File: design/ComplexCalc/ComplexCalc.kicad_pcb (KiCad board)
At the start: 2 copper layers, 111.8 x 112.7 mm, 48 parts, among them J1 V_Battery, J2 Conn_01x09, J3 STLINK, J4 Conn_01x20_Socket, J5 Conn_01x20_Socket, SW1 4, SW10 -, SW11 del, SW12 <-, SW13 7, SW14 8, SW15 9, SW16 M, SW18 MOD, SW19 <, SW2 5, SW20 MOD, SW22 ^, SW23 OK, SW24 v, SW26 MOD, SW27 >, SW28 MOD, SW3 6, SW4 1, SW5 2, SW6 3, SW7 =, SW8 ., SW9 0, U2 AMS1117-3.3, U3 STM32F411CEUx, Y1 8MHz

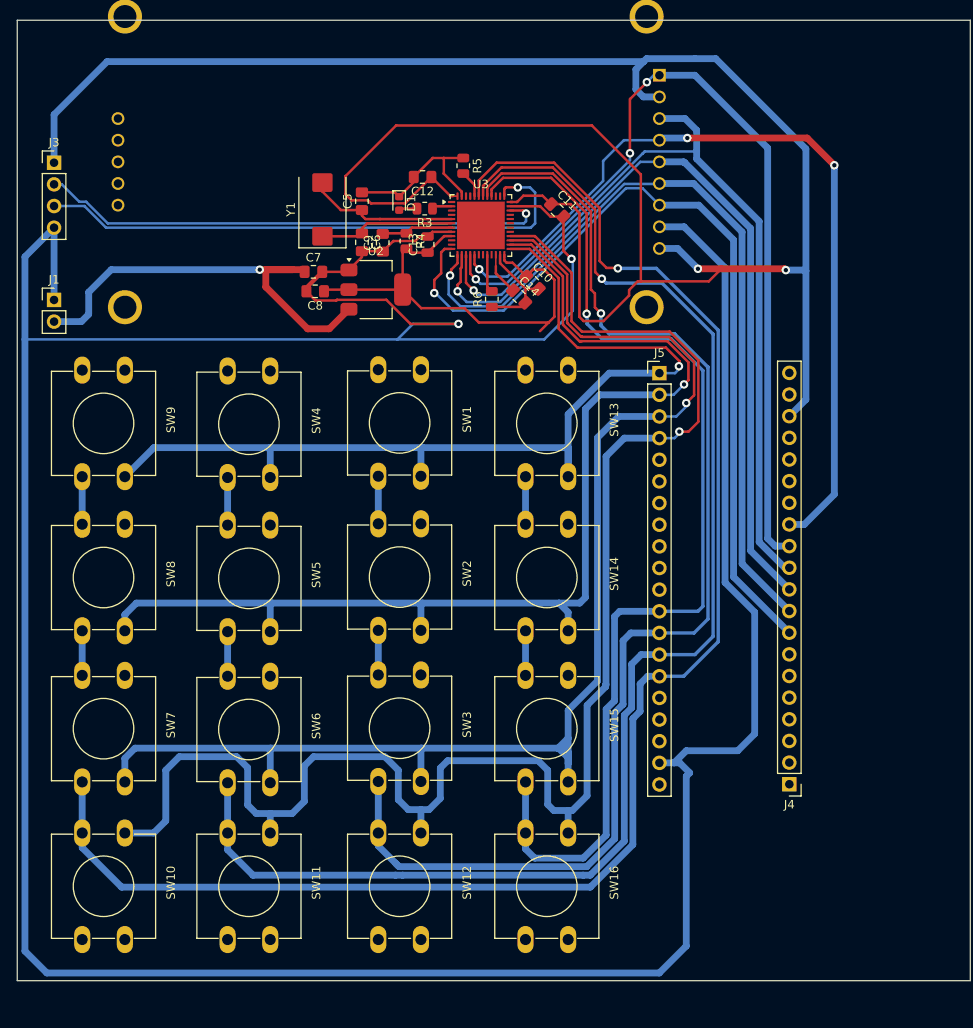
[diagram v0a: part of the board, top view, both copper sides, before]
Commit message: Falta conectar algunas cosas y las resistencias con el ADC
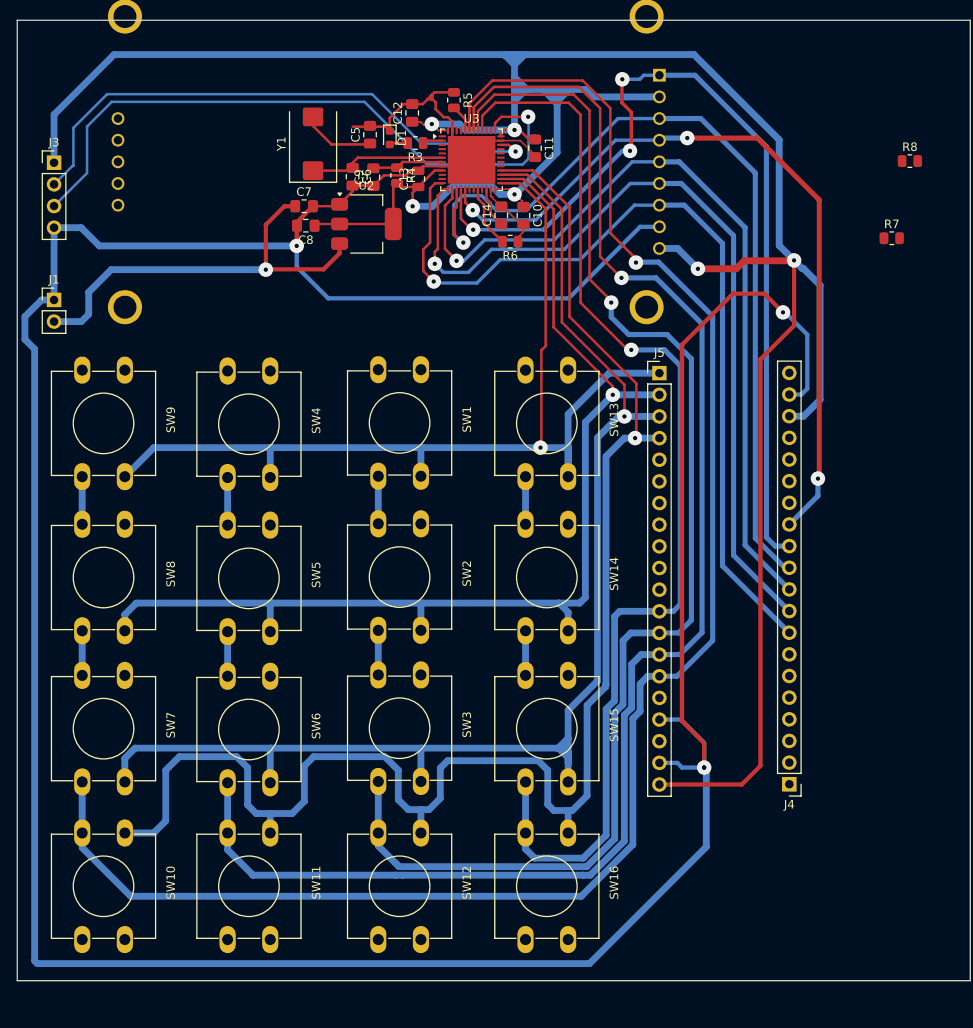
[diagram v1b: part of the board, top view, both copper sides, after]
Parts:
- added R7: 10k, Resistor_SMD:R_0805_2012Metric, F.Cu at (189.2, 27.2)
- added R8: 10k, Resistor_SMD:R_0805_2012Metric, F.Cu at (191.3, 18.2)
- moved C14 9.76 mm to (143.4, 24.6), turned to 90 degrees
- moved C10 7.95 mm to (146.0, 24.6), turned to -90 degrees
- moved C5 7.86 mm to (128.0, 15.1)
- moved C8 7.78 mm to (120.5, 25.8)
- moved R4 7.78 mm to (131.2, 19.9)
- moved C6 7.78 mm to (126.0, 20.0)
- moved C13 7.78 mm to (133.7, 20.3)
- moved C9 7.78 mm to (128.4, 20.1)
- moved D1 7.78 mm to (130.3, 15.5)
- moved R3 7.78 mm to (133.3, 16.1)
- moved U3 7.78 mm to (139.9, 18.1)
- moved Y1 7.78 mm to (121.3, 16.2)
- moved C7 7.78 mm to (120.3, 23.5)
- moved R5 7.78 mm to (137.8, 11.0)
- moved U2 7.78 mm to (127.6, 25.6)
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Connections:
- J4 pad 15: B1 PWM_N -> B1
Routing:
- net 3.3V: track 323.7 -> 346.6 mm, vias 2 -> 6
- net B7: track 196.7 -> 209.1 mm
- net SWCLK: track 66.1 -> 77.2 mm
- net GND: track 440.1 -> 429.0 mm, vias 2 -> 4
- net B6: track 177.1 -> 187.5 mm
- net OSC_IN: track 18.1 -> 8.05 mm
- net B5: track 157.4 -> 166.1 mm
- net A7: track 98.7 -> 90.5 mm
- net B12: track 116.1 -> 123.8 mm
- net SWDIO: track 60.3 -> 66.0 mm
- net B4: track 137.4 -> 143.0 mm
- net B13: track 135.4 -> 130.4 mm
- net A5: track 99.6 -> 104.5 mm
- net B14: track 158.3 -> 154.4 mm
- net A3: track 95.2 -> 98.8 mm
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
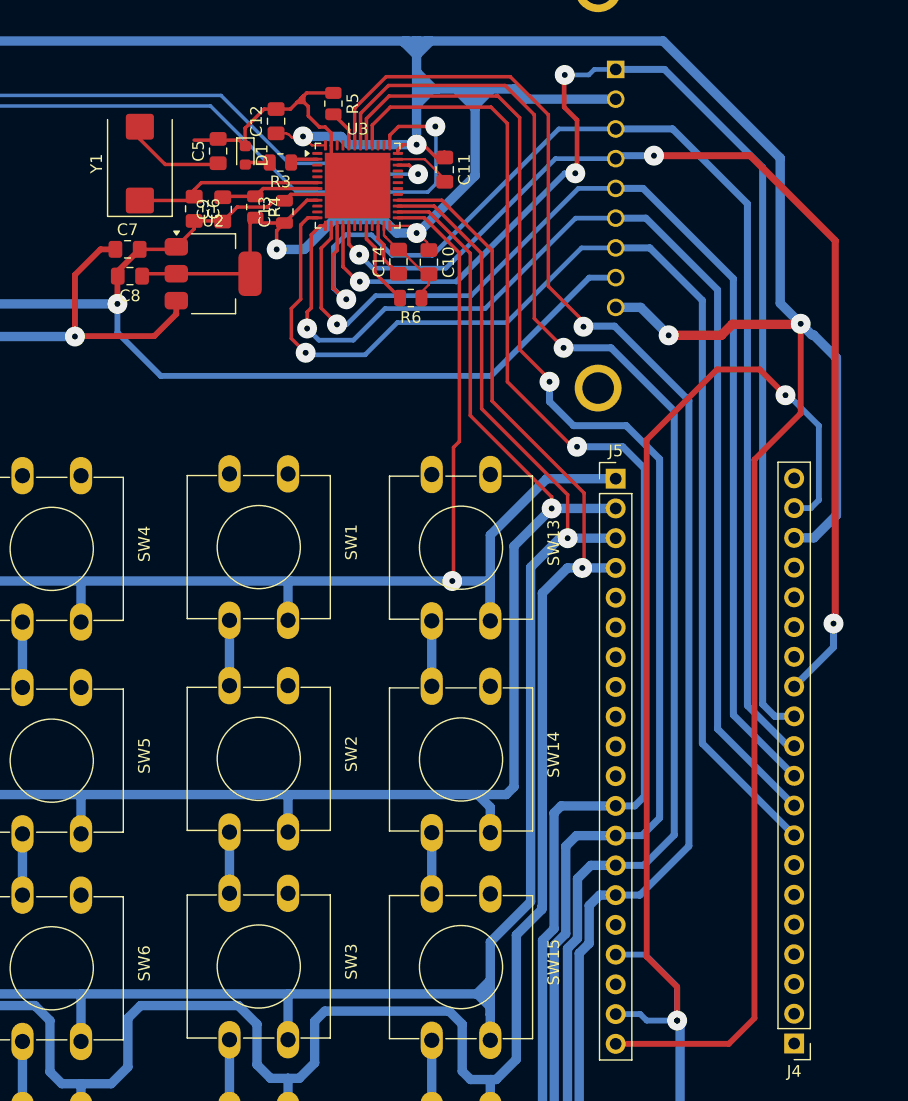
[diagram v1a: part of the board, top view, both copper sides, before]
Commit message: Vias mas grandes
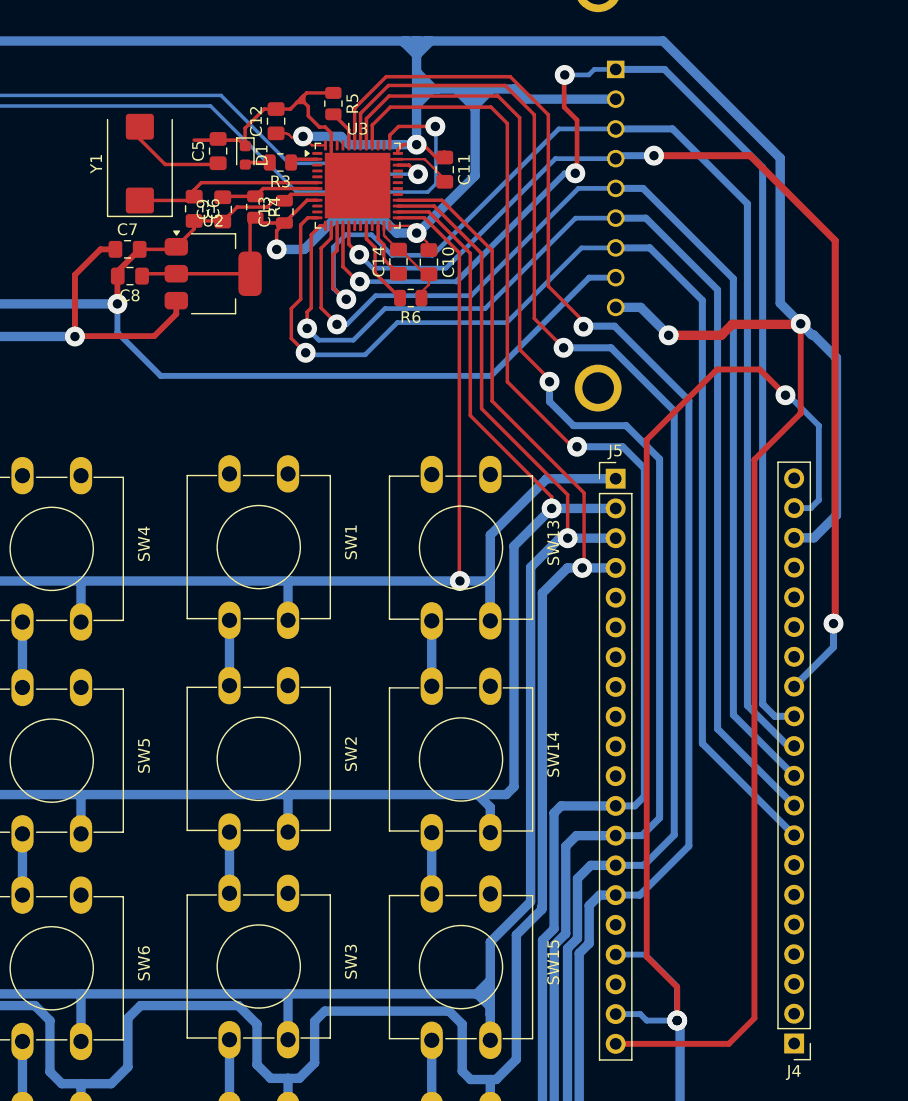
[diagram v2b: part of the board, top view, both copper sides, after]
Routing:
- net B12: track 123.8 -> 123.1 mm
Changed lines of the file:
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@@
 	(via
 		(at 167.2 89.35)
-		(size 1)
-		(drill 0.5)
+		(size 1.7)
+		(drill 0.8)
 		(layers "F.Cu" "B.Cu")
 		(net "GND")
@@
 		(at 176.45 35.95)
 		(size 1.7)
-		(drill 0.5)
+		(drill 0.8)
 		(layers "F.Cu" "B.Cu")
 		(free yes)
@@
 		(at 119.4 28.15)
 		(size 1.7)
-		(drill 0.5)
+		(drill 0.8)
 		(layers "F.Cu" "B.Cu")
 		(free yes)
@@
 		(at 167.2 89.35)
 		(size 1.7)
-		(drill 0.5)
+		(drill 0.8)
 		(layers "F.Cu" "B.Cu")
 		(free yes)
@@
 		(at 133 23.5)
 		(size 1.7)
-		(drill 0.5)
+		(drill 0.8)
 		(layers "F.Cu" "B.Cu")
 		(free yes)
@@
 		(at 166.4716 30.8356)
 		(size 1.7)
-		(drill 0.5)
+		(drill 0.8)
 		(layers "F.Cu" "B.Cu")
 		(net "3.3V")
@@
 		(at 177.75 29.85)
 		(size 1.7)
-		(drill 0.5)
+		(drill 0.8)
 		(layers "F.Cu" "B.Cu")
 		(net "3.3V")
@@
 		(at 144.95 14.55)
 		(size 1.7)
-		(drill 0.5)
+		(drill 0.8)
 		(layers "F.Cu" "B.Cu")
 		(free yes)
@@
 		(at 144.95 22.1)
 		(size 1.7)
-		(drill 0.5)
+		(drill 0.8)
 		(layers "F.Cu" "B.Cu")
 		(free yes)
@@
 		(at 135.25 13.85)
 		(size 1.7)
-		(drill 0.5)
+		(drill 0.8)
 		(layers "F.Cu" "B.Cu")
 		(free yes)
@@
 		(at 157.85 48.1584)
 		(size 1.7)
-		(drill 0.5)
+		(drill 0.8)
 		(layers "F.Cu" "B.Cu")
 		(net "B14")
@@
 		(at 156.3 34.8)
 		(size 1.7)
-		(drill 0.5)
+		(drill 0.8)
 		(layers "F.Cu" "B.Cu")
 		(net "B5")
@@
 		(at 115.7736 30.9372)
 		(size 1.7)
-		(drill 0.5)
+		(drill 0.8)
 		(layers "F.Cu" "B.Cu")
 		(net "VIN")
@@
 		(at 159.1 50.6984)
 		(size 1.7)
-		(drill 0.5)
+		(drill 0.8)
 		(layers "F.Cu" "B.Cu")
 		(net "B15")
@@
 		(at 158.65 40.35)
 		(size 1.7)
-		(drill 0.5)
+		(drill 0.8)
 		(layers "F.Cu" "B.Cu")
 		(net "B4")
@@
 		(at 135.475 32.325)
 		(size 1.7)
-		(drill 0.5)
+		(drill 0.8)
 		(layers "F.Cu" "B.Cu")
 		(net "A2")
@@
 		(at 135.6 30.25)
 		(size 1.7)
-		(drill 0.5)
+		(drill 0.8)
 		(layers "F.Cu" "B.Cu")
 		(net "A3")
@@
 		(at 138.15 29.9)
 		(size 1.7)
-		(drill 0.5)
+		(drill 0.8)
 		(layers "F.Cu" "B.Cu")
 		(net "A4")
@@
 		(at 138.943978 27.757854)
 		(size 1.7)
-		(drill 0.5)
+		(drill 0.8)
 		(layers "F.Cu" "B.Cu")
 		(net "A5")
@@
 		(at 158.5 16.998)
 		(size 1.7)
-		(drill 0.5)
+		(drill 0.8)
 		(layers "F.Cu" "B.Cu")
 		(net "A6")
@@
 		(at 140.1 26.25)
 		(size 1.7)
-		(drill 0.5)
+		(drill 0.8)
 		(layers "F.Cu" "B.Cu")
 		(net "A6")
@@
 		(at 157.6 8.6)
 		(size 1.7)
-		(drill 0.5)
+		(drill 0.8)
 		(layers "F.Cu" "B.Cu")
 		(net "A6")
@@
 		(at 165.2192 15.494)
 		(size 1.7)
-		(drill 0.5)
+		(drill 0.8)
 		(layers "F.Cu" "B.Cu")
 		(net "A7")
@@
 		(at 180.55 55.45)
 		(size 1.7)
-		(drill 0.5)
+		(drill 0.8)
 		(layers "F.Cu" "B.Cu")
 		(net "A7")
@@
 		(at 140.05 23.95)
 		(size 1.7)
-		(drill 0.5)
+		(drill 0.8)
 		(layers "F.Cu" "B.Cu")
 		(net "A7")
@@
 	)
 	(segment
-		(start 145.609644 20.8)
-		(end 143.35 20.8)
-		(width 0.3)
-		(layer "F.Cu")
-		(net "B12")
-	)
-	(segment
-		(start 148.1 40.4)
-		(end 148.6 39.9)
-		(width 0.3)
-		(layer "F.Cu")
-		(net "B12")
-	)
-	(segment
-		(start 148 51.816)
-		(end 148.1 51.716)
-		(width 0.3)
-		(layer "F.Cu")
-		(net "B12")
-	)
-	(segment
-		(start 148.1 51.716)
-		(end 148.1 40.4)
+		(start 148.6 51.416)
+		(end 148.6 23.790356)
 		(width 0.3)
 		(layer "F.Cu")
@@
 	)
 	(segment
-		(start 148.6 39.9)
-		(end 148.6 23.790356)
+		(start 145.609644 20.8)
+		(end 143.35 20.8)
 		(width 0.3)
 		(layer "F.Cu")
@@
 	)
 	(via
-		(at 148 51.816)
+		(at 148.65 51.816)
 		(size 1.7)
-		(drill 0.5)
+		(drill 0.8)
 		(layers "F.Cu" "B.Cu")
 		(net "B12")
@@
 		(at 156.4816 45.6184)
 		(size 1.7)
-		(drill 0.5)
+		(drill 0.8)
 		(layers "F.Cu" "B.Cu")
 		(net "B13")
@@
 		(at 145.07435 17.07435)
 		(size 1.7)
-		(drill 0.5)
+		(drill 0.8)
 		(layers "F.Cu" "B.Cu")
 		(net "SWDIO")
@@
 		(at 146.5516 13.0016)
 		(size 1.7)
-		(drill 0.5)
+		(drill 0.8)
 		(layers "F.Cu" "B.Cu")
 		(net "SWCLK")
@@
 		(at 157.5 31.9)
 		(size 1.7)
-		(drill 0.5)
+		(drill 0.8)
 		(layers "F.Cu" "B.Cu")
 		(net "B6")
@@
 		(at 159.2 30.1)
 		(size 1.7)
-		(drill 0.5)
+		(drill 0.8)
 		(layers "F.Cu" "B.Cu")
 		(net "B7")

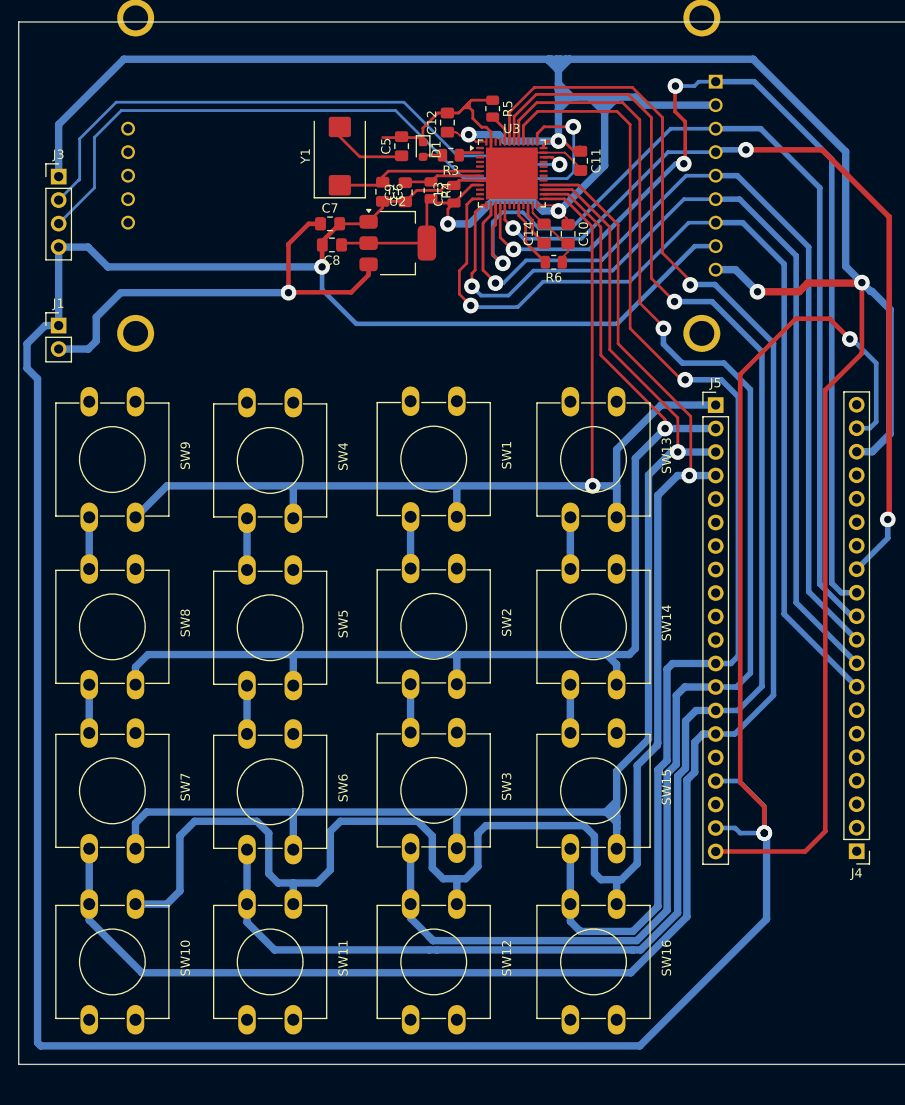
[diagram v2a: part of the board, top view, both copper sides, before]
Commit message: Sigue faltando el adc
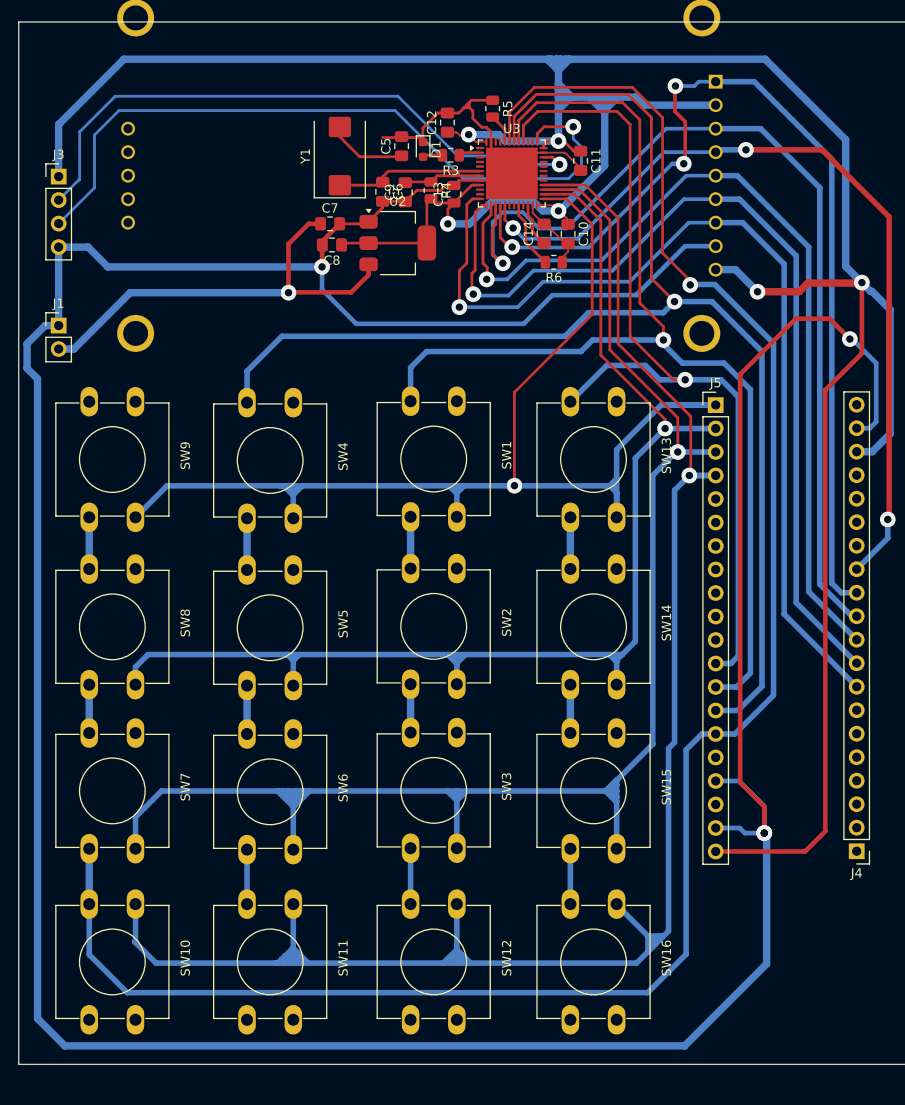
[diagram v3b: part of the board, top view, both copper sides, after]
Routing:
- net B4: track 143.0 -> 113.7 mm
- net B5: track 166.1 -> 137.8 mm
- net B6: track 187.5 -> 164.0 mm
- net B14: track 154.4 -> 174.3 mm
- net B15: track 185.2 -> 201.4 mm
- net B12: track 123.1 -> 134.7 mm
- net B13: track 130.4 -> 136.8 mm
- net B7: track 209.1 -> 215.4 mm
- net VIN: track 49.1 -> 47.6 mm
- net GND: track 429.0 -> 430.4 mm
- net SWDIO: track 66.0 -> 66.9 mm
- net SWCLK: track 77.2 -> 78.2 mm
- net A2: track 101.9 -> 102.8 mm
- net 3.3V: track 346.6 -> 347.3 mm
- net A6: track 106.3 -> 105.7 mm

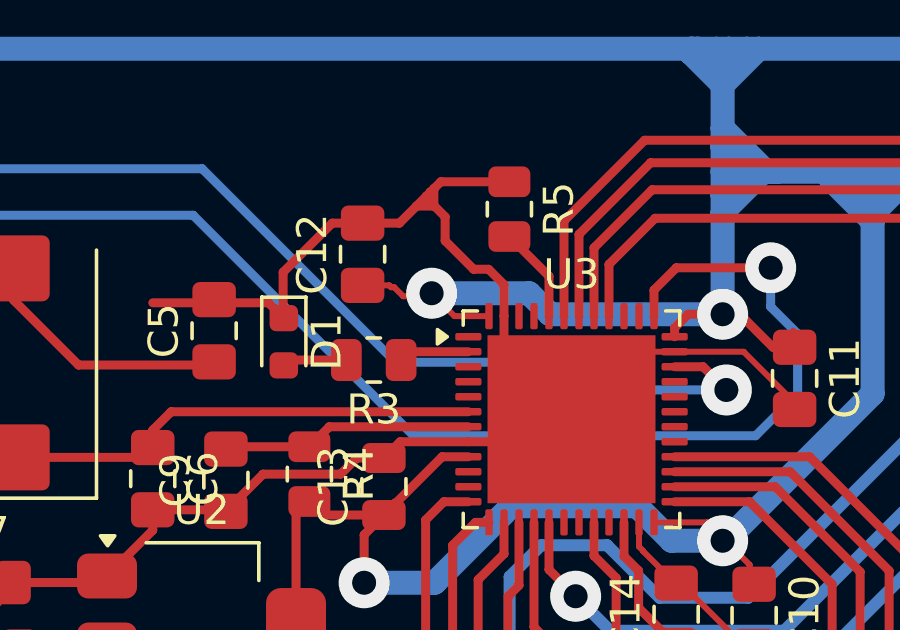
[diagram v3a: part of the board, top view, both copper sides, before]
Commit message: Fixxed capacitors values C14,C9 and VBAT to 3.3 V
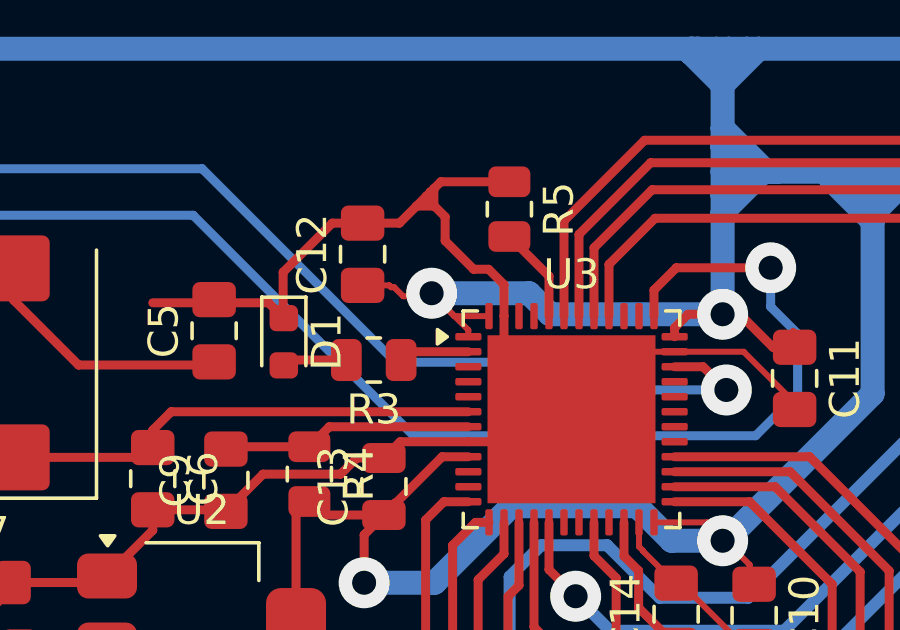
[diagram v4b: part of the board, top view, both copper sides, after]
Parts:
- C14: value 2.2uF -> 4.7uF
- C9: value 1uF -> 100nF
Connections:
- U3 pad 1: VBAT -> 3.3V
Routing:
- net 3.3V: track 347.3 -> 349.3 mm
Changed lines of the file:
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@@
 			)
 		)
-		(property "Value" "1uF"
+		(property "Value" "100nF"
 			(at 0 1.68 90)
 			(layer "F.Fab")
@@
 			(layers "F.Cu" "F.Mask" "F.Paste")
 			(roundrect_rratio 0.25)
-			(net "VBAT")
+			(net "3.3V")
 			(pinfunction "VBAT_1")
 			(pintype "power_in")
@@
 			)
 		)
-		(property "Value" "2.2uF"
+		(property "Value" "4.7uF"
 			(at 0 1.679999 90)
 			(layer "F.Fab")
@@
 	)
 	(segment
+		(start 136.475 15.075)
+		(end 135.25 13.85)
+		(width 0.2)
+		(layer "F.Cu")
+		(net "3.3V")
+	)
+	(segment
 		(start 142.6625 21.4875)
 		(end 144.4375 21.4875)
@@
 		(layer "F.Cu")
 		(net "3.3V")
+	)
+	(segment
+		(start 136.475 15.3)
+		(end 136.475 15.075)
+		(width 0.2)
+		(layer "F.Cu")
+		(net "3.3V")
